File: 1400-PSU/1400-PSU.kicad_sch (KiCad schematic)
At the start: 38 parts, among them J1 Battery, J2 Charger, J3 MAINBOARD_OUT, Q1 IRF9540N, SW1 SW_DPST, U3 LM7805_TO220, U4 7812

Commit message: Generated gerbers.
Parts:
- removed J2: Charger, Connector_BarrelJack:BarrelJack_CUI_PJ-063AH_Horizontal, symbol Connector:Conn_01x02_Socket
- added F1: 3A, Fuse:Fuseholder_Blade_Mini_Keystone_3568, symbol Device:Fuse
- added J2: Jack-DC, Connector_BarrelJack:BarrelJack_CUI_PJ-063AH_Horizontal, symbol Connector:Jack-DC
- added NT1, NT2, NT3: NetTie_2, NetTie:NetTie-2_SMD_Pad2.0mm, symbol Device:NetTie_2
- C1: footprint Capacitor_THT:CP_Radial_D10.0mm_P5.00mm -> Capacitor_THT:CP_Radial_D8.0mm_P3.50mm
- C3: footprint Capacitor_THT:C_Disc_D4.7mm_W2.5mm_P5.00mm -> Capacitor_THT:C_Disc_D5.1mm_W3.2mm_P5.00mm
- C4: value 22uF 25V -> 0.1uF; footprint Capacitor_THT:CP_Radial_D6.3mm_P2.50mm -> Capacitor_THT:C_Disc_D5.1mm_W3.2mm_P5.00mm
- C8: value 10uF 50V -> 0.22uF; footprint Capacitor_THT:CP_Radial_D8.0mm_P5.00mm -> Capacitor_THT:C_Disc_D5.1mm_W3.2mm_P5.00mm
- D1, D4: value 1N4001 -> 31DQ06
- D2: value 1N4001 -> 31D106
- U3: footprint Package_TO_SOT_THT:TO-220-3_Vertical -> Package_TO_SOT_THT:TO-220-3_Horizontal_TabDown
- U4: value 7812 -> LM340T-12; footprint Package_TO_SOT_THT:TO-220-3_Vertical -> Package_TO_SOT_THT:TO-220-3_Horizontal_TabDown
- U5: value ~ -> N7812-1PH; footprint Package_TO_SOT_THT:TO-220-3_Vertical -> Package_TO_SOT_THT:TO-220-3_Horizontal_TabDown
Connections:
- net BATT_SENSE: now also NT2.2; no longer D1.2 (A), Q1.2 (D)
- net GND: now also J2.2
- net POWER_BRICK: now also F1.1, NT1.1, NT3.2; no longer R1.2, R2.1, R8.1
- new net: D1.2 (A), NT2.1, Q1.2 (D)
- new net: NT1.2, R1.2, R2.1
- new net: F1.2, J2.1
- new net CHARGER_SENSE: NT3.1, R8.1
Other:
- moved on the sheet: D4

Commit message: Updating for next board revision.
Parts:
- added H1, H2, H3, H4: ~, MountingHole:MountingHole_3.5mm_Pad_TopBottom, symbol Mechanical:MountingHole_Pad
- added JP3: LOW_BATT, Jumper:SolderJumper-2_P1.3mm_Open_RoundedPad1.0x1.5mm, symbol Jumper:SolderJumper_2_Open
- added JP4: REALLY_LOW_BATT, Jumper:SolderJumper-2_P1.3mm_Open_RoundedPad1.0x1.5mm, symbol Jumper:SolderJumper_2_Open
- C2: value 220uF 50V -> 47uF 50V
- D1: footprint Diode_THT:D_DO-41_SOD81_P10.16mm_Horizontal -> Diode_THT:D_DO-201AD_P5.08mm_Vertical_AnodeUp
- D2: footprint Diode_THT:D_DO-41_SOD81_P10.16mm_Horizontal -> Diode_THT:D_DO-201AD_P5.08mm_Vertical_KathodeUp
- D4: footprint Diode_THT:D_DO-41_SOD81_P10.16mm_Horizontal -> Diode_THT:D_DO-201AD_P12.70mm_Horizontal
- R4: value 1k -> 20k
- R6: value 20k -> 1k
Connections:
- net -22_RAIL: now also C3.2, U1.4 (GND)
- net GND: now also L1.1, H1.1, H2.1, H3.1, H4.1; no longer C3.2, U1.4 (GND)
- net LOW_BATT: now also JP3.1 (A)
- net REALLY_LOW_BATT: now also JP4.1 (A)
- net at L1.2, U1.2 (Switch_Emiiter): now also D3.1 (K)
- net at A1.30 (VIN), JP2.2 (C): now also JP3.2 (B), JP4.2 (B)
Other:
- moved on the sheet: A1, C4, C5, C6, C7, C8, C9, JP1, R4, R5, R6, R7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

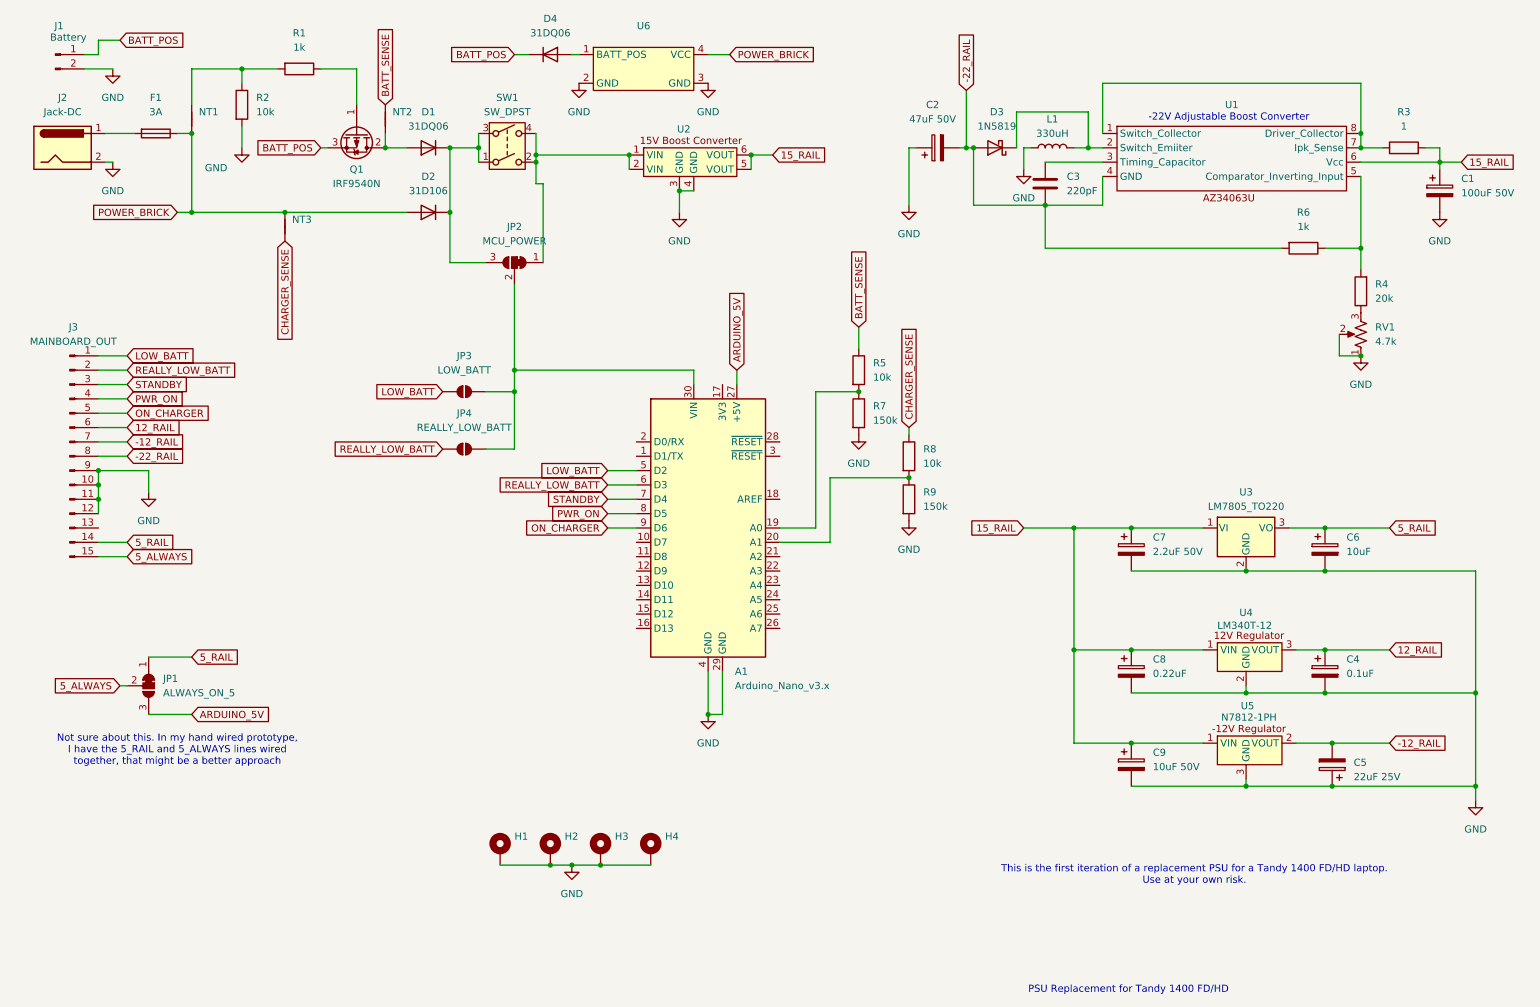
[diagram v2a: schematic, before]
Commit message: Update to readme and BOM.
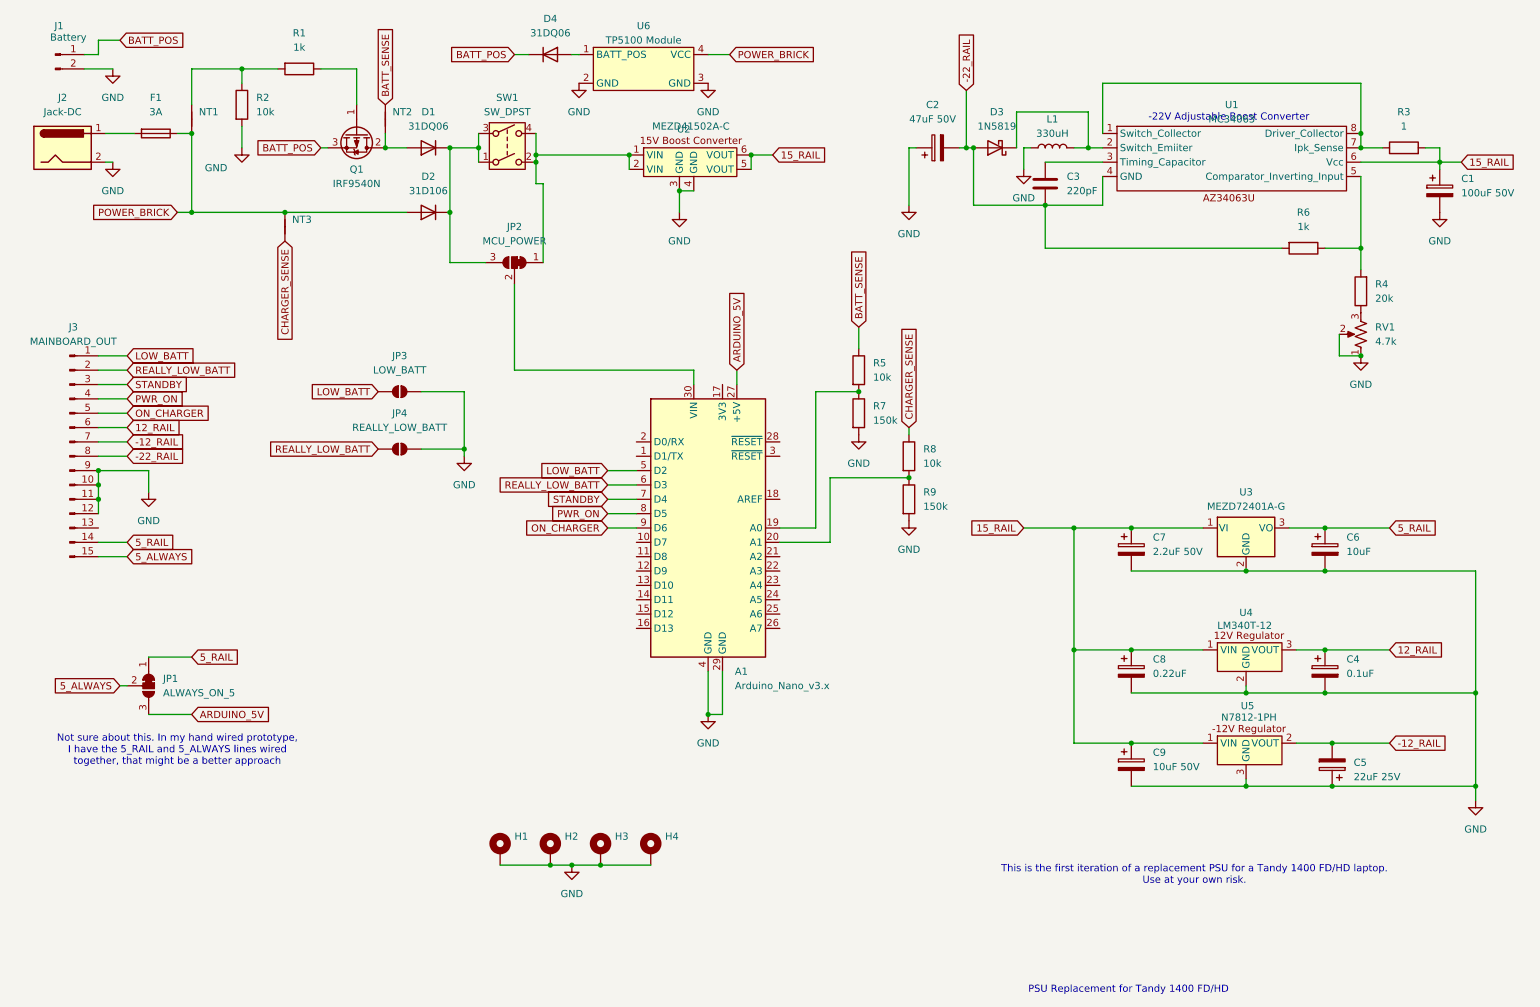
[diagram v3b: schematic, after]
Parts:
- U1: value ~ -> MC34063
- U2: value ~ -> MEZD41502A-C
- U3: value LM7805_TO220 -> MEZD72401A-G
- U6: value ~ -> TP5100 Module
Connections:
- net GND: now also JP3.2 (B), JP4.2 (B)
- net at A1.30 (VIN), JP2.2 (C): no longer JP3.2 (B), JP4.2 (B)
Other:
- moved on the sheet: JP3, JP4
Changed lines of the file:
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@@
 	)
 	(junction
+		(at 88.9 93.98)
+		(diameter 0)
+		(color 0 0 0 0)
+	)
+	(junction
 		(at 247.65 38.1)
 		(diameter 0)
@@
 	)
 	(junction
-		(at 97.79 83.82)
-		(diameter 0)
-		(color 0 0 0 0)
-	)
-	(junction
 		(at 118.11 41.91)
 		(diameter 0)
@@
 	)
 	(junction
-		(at 97.79 80.01)
-		(diameter 0)
-		(color 0 0 0 0)
-	)
-	(junction
 		(at 104.14 167.64)
 		(diameter 0)
@@
 	(wire
 		(pts
-			(xy 97.79 83.82) (xy 97.79 80.01)
-		)
-		(stroke
-			(width 0)
-			(type default)
-		)
-	)
-	(wire
-		(pts
 			(xy 24.13 21.59) (xy 24.13 24.13)
 		)
@@
 	(wire
 		(pts
+			(xy 81.28 93.98) (xy 88.9 93.98)
+		)
+		(stroke
+			(width 0)
+			(type default)
+		)
+	)
+	(wire
+		(pts
 			(xy 247.65 45.72) (xy 247.65 58.42)
 		)
@@
 	(wire
 		(pts
-			(xy 92.71 83.82) (xy 97.79 83.82)
-		)
-		(stroke
-			(width 0)
-			(type default)
-		)
-	)
-	(wire
-		(pts
 			(xy 139.7 41.91) (xy 139.7 44.45)
 		)
@@
 	(wire
 		(pts
-			(xy 207.01 107.95) (xy 219.71 107.95)
+			(xy 81.28 83.82) (xy 88.9 83.82)
 		)
 		(stroke
@@
 	(wire
 		(pts
-			(xy 40.64 26.67) (xy 49.53 26.67)
+			(xy 207.01 107.95) (xy 219.71 107.95)
 		)
 		(stroke
@@
 	(wire
 		(pts
-			(xy 252.73 146.05) (xy 242.57 146.05)
+			(xy 40.64 26.67) (xy 49.53 26.67)
 		)
 		(stroke
@@
 	(wire
 		(pts
-			(xy 24.13 82.55) (xy 29.21 82.55)
+			(xy 252.73 146.05) (xy 242.57 146.05)
 		)
 		(stroke
@@
 	(wire
 		(pts
-			(xy 97.79 93.98) (xy 97.79 83.82)
+			(xy 24.13 82.55) (xy 29.21 82.55)
 		)
 		(stroke
@@
 	(wire
 		(pts
+			(xy 88.9 83.82) (xy 88.9 93.98)
+		)
+		(stroke
+			(width 0)
+			(type default)
+		)
+	)
+	(wire
+		(pts
 			(xy 33.02 140.97) (xy 40.64 140.97)
 		)
@@
 	(wire
 		(pts
+			(xy 88.9 93.98) (xy 88.9 95.25)
+		)
+		(stroke
+			(width 0)
+			(type default)
+		)
+	)
+	(wire
+		(pts
 			(xy 86.36 40.64) (xy 91.44 40.64)
 		)
@@
 	(wire
 		(pts
-			(xy 92.71 93.98) (xy 97.79 93.98)
-		)
-		(stroke
-			(width 0)
-			(type default)
-		)
-	)
-	(wire
-		(pts
 			(xy 153.67 110.49) (xy 144.78 110.49)
 		)
@@
 	(global_label "REALLY_LOW_BATT"
 		(shape input)
-		(at 85.09 93.98 180)
+		(at 73.66 93.98 180)
 		(fields_autoplaced yes)
 		(effects
@@
 		)
 		(property "Intersheetrefs" "${INTERSHEET_REFS}"
-			(at 65.4134 93.98 0)
+			(at 53.9834 93.98 0)
 			(effects
 				(font
@@
 	(global_label "LOW_BATT"
 		(shape input)
-		(at 85.09 83.82 180)
+		(at 73.66 83.82 180)
 		(fields_autoplaced yes)
 		(effects
@@
 		)
 		(property "Intersheetrefs" "${INTERSHEET_REFS}"
-			(at 73.0334 83.82 0)
+			(at 61.6034 83.82 0)
 			(effects
 				(font
@@
 	(symbol
 		(lib_id "Jumper:SolderJumper_2_Open")
-		(at 88.9 83.82 0)
+		(at 77.47 83.82 0)
 		(unit 1)
 		(exclude_from_sim yes)
@@
 		(fields_autoplaced yes)
 		(property "Reference" "JP3"
-			(at 88.9 77.47 0)
+			(at 77.47 77.47 0)
 			(effects
 				(font
@@
 		)
 		(property "Value" "LOW_BATT"
-			(at 88.9 80.01 0)
+			(at 77.47 80.01 0)
 			(effects
 				(font
@@
 		)
 		(property "Footprint" "Jumper:SolderJumper-2_P1.3mm_Open_RoundedPad1.0x1.5mm"
-			(at 88.9 83.82 0)
+			(at 77.47 83.82 0)
 			(effects
 				(font
@@
 		)
 		(property "Datasheet" "~"
-			(at 88.9 83.82 0)
+			(at 77.47 83.82 0)
 			(effects
 				(font
@@
 		)
 		(property "Description" "Solder Jumper, 2-pole, open"
-			(at 88.9 83.82 0)
+			(at 77.47 83.82 0)
 			(effects
 				(font
@@
 	(symbol
 		(lib_id "power:GND")
+		(at 88.9 95.25 0)
+		(unit 1)
+		(exclude_from_sim no)
+		(in_bom yes)
+		(on_board yes)
+		(dnp no)
+		(fields_autoplaced yes)
+		(property "Reference" "#PWR017"
+			(at 88.9 101.6 0)
+			(effects
+				(font
+					(size 1.27 1.27)
+				)
+				(hide yes)
+			)
+		)
+		(property "Value" "GND"
+			(at 88.9 100.33 0)
+			(effects
+				(font
+					(size 1.27 1.27)
+				)
+			)
+		)
+		(property "Footprint" ""
+			(at 88.9 95.25 0)
+			(effects
+				(font
+					(size 1.27 1.27)
+				)
+				(hide yes)
+			)
+		)
+		(property "Datasheet" ""
+			(at 88.9 95.25 0)
+			(effects
+				(font
+					(size 1.27 1.27)
+				)
+				(hide yes)
+			)
+		)
+		(property "Description" "Power symbol creates a global label with name \"GND\" , ground"
+			(at 88.9 95.25 0)
+			(effects
+				(font
+					(size 1.27 1.27)
+				)
+				(hide yes)
+			)
+		)
+		(pin "1"
+		)
+		(instances
+			(project ""
+				(path "/1e170452-a7b5-4944-9251-2ce18f45a364"
+					(reference "#PWR017")
+					(unit 1)
+				)
+			)
+		)
+	)
+	(symbol
+		(lib_id "power:GND")
 		(at 167.64 106.68 0)
 		(unit 1)
@@
 			)
 		)
-		(property "Value" "~"
+		(property "Value" "MC34063"
 			(at 224.79 35.56 0)
 			(effects
@@
 			)
 		)
-		(property "Value" "~"
+		(property "Value" "TP5100 Module"
 			(at 120.65 21.59 0)
 			(effects
@@
 			)
 		)
-		(property "Value" "LM7805_TO220"
+		(property "Value" "MEZD72401A-G"
 			(at 227.33 104.14 0)
 			(effects
@@
 	(symbol
 		(lib_id "Jumper:SolderJumper_2_Open")
-		(at 88.9 93.98 0)
+		(at 77.47 93.98 0)
 		(unit 1)
 		(exclude_from_sim yes)
@@
 		(fields_autoplaced yes)
 		(property "Reference" "JP4"
-			(at 88.9 87.63 0)
+			(at 77.47 87.63 0)
 			(effects
 				(font
@@
 		)
 		(property "Value" "REALLY_LOW_BATT"
-			(at 88.9 90.17 0)
+			(at 77.47 90.17 0)
 			(effects
 				(font
@@
 		)
 		(property "Footprint" "Jumper:SolderJumper-2_P1.3mm_Open_RoundedPad1.0x1.5mm"
-			(at 88.9 93.98 0)
+			(at 77.47 93.98 0)
 			(effects
 				(font
@@
 		)
 		(property "Datasheet" "~"
-			(at 88.9 93.98 0)
+			(at 77.47 93.98 0)
 			(effects
 				(font
@@
 		)
 		(property "Description" "Solder Jumper, 2-pole, open"
-			(at 88.9 93.98 0)
+			(at 77.47 93.98 0)
 			(effects
 				(font
@@
 			)
 		)
-		(property "Value" "~"
+		(property "Value" "MEZD41502A-C"
 			(at 129.032 36.83 0)
 			(effects
